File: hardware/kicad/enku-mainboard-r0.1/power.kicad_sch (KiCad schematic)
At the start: 5 parts

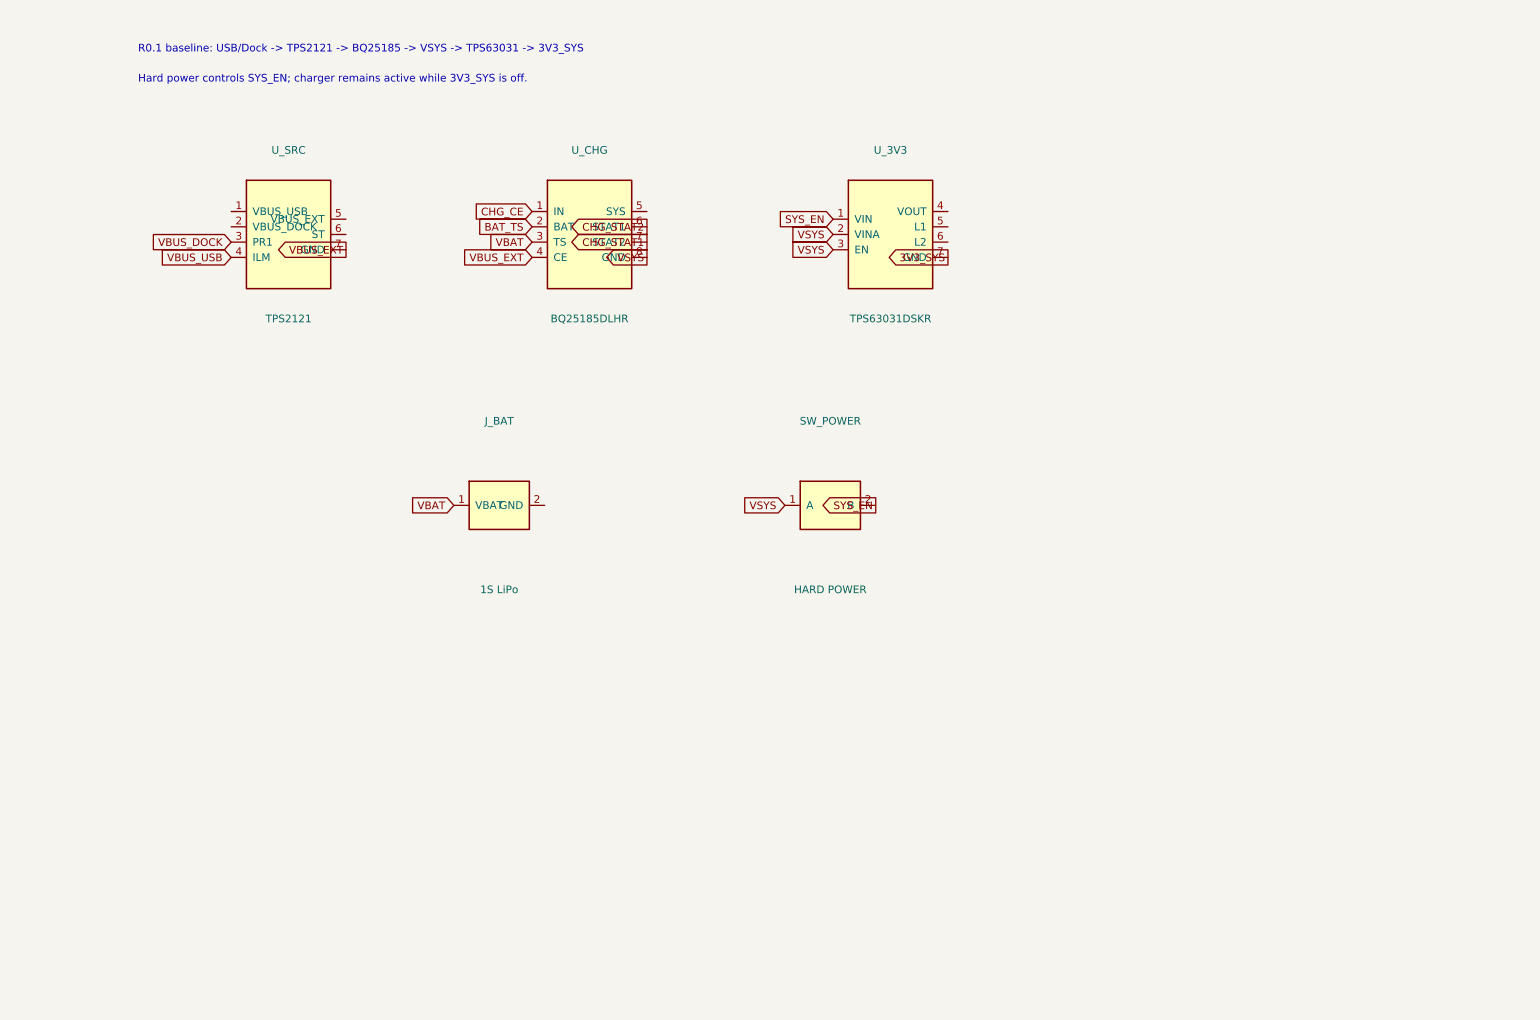
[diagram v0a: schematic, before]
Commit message: Expand R0.1 power sheet to exact IC pins and passives
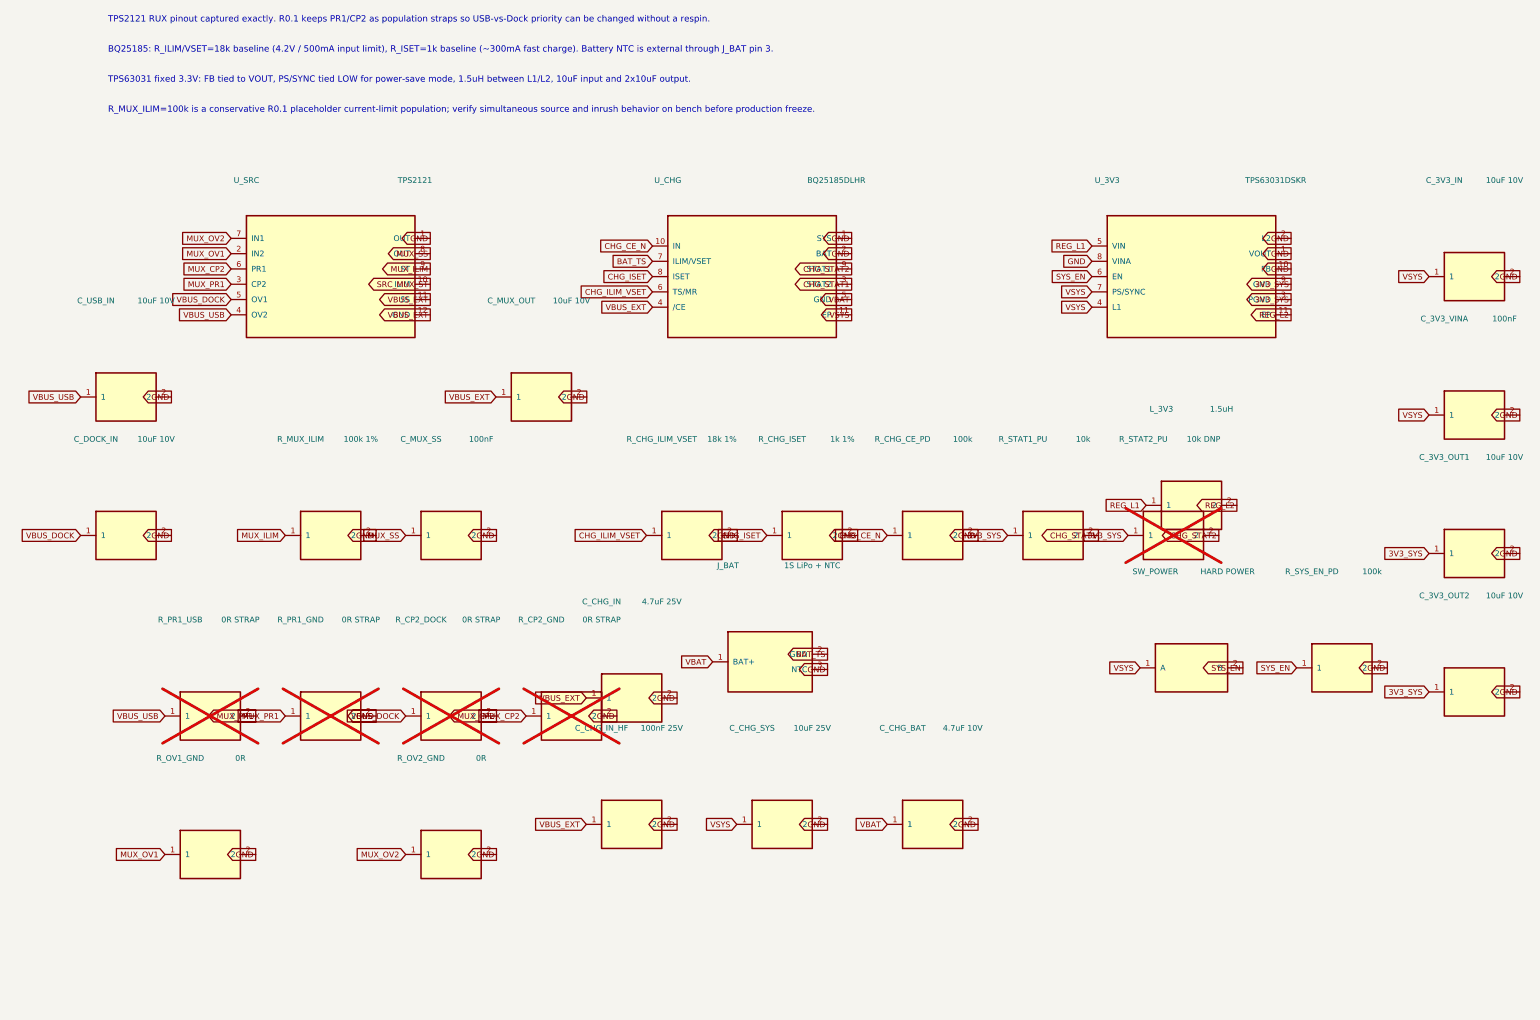
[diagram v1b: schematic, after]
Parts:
- removed J_BAT: 1S LiPo, Connector_JST:JST_PH_S2B-PH-SM4-TB_1x02-1MP_P2.00mm_Horizontal, symbol ENKU:BATTERY_2P
- removed SW_POWER: HARD POWER, Button_Switch_SMD:SW_SPDT_CK_JS102011SAQN, symbol ENKU:POWER_SWITCH
- removed U_3V3: TPS63031DSKR, Package_SON:WSON-10-1EP_2.5x2.5mm_P0.5mm_EP0.8x2mm, symbol ENKU:TPS63031_BLOCK
- removed U_CHG: BQ25185DLHR, Package_SON:Texas_DLH0010A, symbol ENKU:BQ25185_BLOCK
- removed U_SRC: TPS2121, Package_DFN_QFN:VQFN-HR-12-1EP_2.5x2.0mm_P0.5mm_EP0.6x1.6mm, symbol ENKU:TPS2121_BLOCK
- added C_3V3_IN, C_3V3_OUT1, C_3V3_OUT2, C_DOCK_IN, C_MUX_OUT, C_USB_IN: 10uF 10V, Capacitor_SMD:C_0805_2012Metric, symbol ENKU:C
- added C_3V3_VINA, C_MUX_SS: 100nF, Capacitor_SMD:C_0603_1608Metric, symbol ENKU:C
- added C_CHG_BAT: 4.7uF 10V, Capacitor_SMD:C_0805_2012Metric, symbol ENKU:C
- added C_CHG_IN: 4.7uF 25V, Capacitor_SMD:C_0805_2012Metric, symbol ENKU:C
- added C_CHG_IN_HF: 100nF 25V, Capacitor_SMD:C_0603_1608Metric, symbol ENKU:C
- added C_CHG_SYS: 10uF 25V, Capacitor_SMD:C_0805_2012Metric, symbol ENKU:C
- added J_BAT: 1S LiPo + NTC, Connector_Generic:Conn_01x03, symbol ENKU:BAT3
- added L_3V3: 1.5uH, Inductor_SMD:L_2520_HandSoldering, symbol ENKU:L
- added R_CHG_CE_PD, R_SYS_EN_PD: 100k, Resistor_SMD:R_0603_1608Metric, symbol ENKU:R
- added R_CHG_ILIM_VSET: 18k 1%, Resistor_SMD:R_0603_1608Metric, symbol ENKU:R
- added R_CHG_ISET: 1k 1%, Resistor_SMD:R_0603_1608Metric, symbol ENKU:R
- added R_CP2_DOCK, R_CP2_GND, R_PR1_GND, R_PR1_USB: 0R STRAP, Resistor_SMD:R_0603_1608Metric, symbol ENKU:R
- added R_MUX_ILIM: 100k 1%, Resistor_SMD:R_0603_1608Metric, symbol ENKU:R
- added R_OV1_GND, R_OV2_GND: 0R, Resistor_SMD:R_0603_1608Metric, symbol ENKU:R
- added R_STAT1_PU: 10k, Resistor_SMD:R_0603_1608Metric, symbol ENKU:R
- added R_STAT2_PU: 10k DNP, Resistor_SMD:R_0603_1608Metric, symbol ENKU:R
- added SW_POWER: HARD POWER, Button_Switch_SMD:SW_SPST, symbol ENKU:SW_SPST
- added U_3V3: TPS63031DSKR, ENKU:TPS63031_DSK0010A, symbol ENKU:TPS63031_DSK
- added U_CHG: BQ25185DLHR, ENKU:BQ25185_DLH0010A, symbol ENKU:BQ25185_DLH
- added U_SRC: TPS2121, ENKU:TPS2121_RUX0012B, symbol ENKU:TPS2121_RUX
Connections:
- net 3V3_SYS: now also C_3V3_OUT1.1, C_3V3_OUT2.1, R_STAT1_PU.1, R_STAT2_PU.1, U_3V3.3 (PGND), U_3V3.9 (GND)
- net BAT_TS: now also J_BAT.2 (GND), U_CHG.7 (ILIM/VSET)
- net CHG_STAT1: now also R_STAT1_PU.2, U_CHG.3 (STAT2)
- net CHG_STAT2: now also R_STAT2_PU.2, U_CHG.9 (STAT1)
- net SYS_EN: now also R_SYS_EN_PD.1, SW_POWER.2 (B), U_3V3.6 (EN)
- net VBAT: now also C_CHG_BAT.1, J_BAT.1 (BAT+), U_CHG.5 (GND)
- net VBUS_DOCK: now also C_DOCK_IN.1, R_CP2_DOCK.1, U_SRC.5 (OV1)
- net VBUS_EXT: now also C_CHG_IN.1, C_CHG_IN_HF.1, C_MUX_OUT.1, U_CHG.4 (/CE), U_SRC.11 (SS), U_SRC.12 (GND)
- net VBUS_USB: now also C_USB_IN.1, R_PR1_USB.1, U_SRC.4 (OV2)
- net VSYS: now also C_3V3_IN.1, C_3V3_VINA.1, C_CHG_SYS.1, SW_POWER.1 (A), U_3V3.4 (L1), U_3V3.7 (PS/SYNC), U_CHG.11 (EP)
- new net CHG_CE_N: R_CHG_CE_PD.1, U_CHG.10 (IN)
- new net CHG_ILIM_VSET: R_CHG_ILIM_VSET.1, U_CHG.6 (TS/MR)
- new net CHG_ISET: R_CHG_ISET.1, U_CHG.8 (ISET)
- new net GND: C_3V3_IN.2, C_3V3_OUT1.2, C_3V3_OUT2.2, C_3V3_VINA.2, C_CHG_BAT.2, C_CHG_IN.2, C_CHG_IN_HF.2, C_CHG_SYS.2, C_DOCK_IN.2, C_MUX_OUT.2, C_MUX_SS.2, C_USB_IN.2, J_BAT.3 (NTC), R_CHG_CE_PD.2, R_CHG_ILIM_VSET.2, R_CHG_ISET.2, R_CP2_GND.2, R_MUX_ILIM.2, R_OV1_GND.2, R_OV2_GND.2, R_PR1_GND.2, R_SYS_EN_PD.2, U_3V3.1 (VOUT), U_3V3.10 (FB), U_3V3.2 (L2), U_3V3.8 (VINA), U_CHG.1 (SYS), U_CHG.2 (BAT), U_SRC.1 (OUT)
- new net MUX_CP2: R_CP2_DOCK.2, R_CP2_GND.1, U_SRC.6 (PR1)
- new net MUX_ILIM: R_MUX_ILIM.1, U_SRC.9 (ST)
- new net MUX_OV1: R_OV1_GND.1, U_SRC.2 (IN2)
- new net MUX_OV2: R_OV2_GND.1, U_SRC.7 (IN1)
- new net MUX_PR1: R_PR1_GND.1, R_PR1_USB.2, U_SRC.3 (CP2)
- new net MUX_SS: C_MUX_SS.1, U_SRC.8 (OUT)
- new net REG_L1: L_3V3.1, U_3V3.5 (VIN)
- new net REG_L2: L_3V3.2, U_3V3.11 (EP)
- new net SRC_MUX_ST: U_SRC.10 (ILIM)
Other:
- note added: "BQ25185: R_ILIM/VSET=18k baseline (4.2V / 500mA input limit), R_ISET=1k baseline (~300mA fast charge). Battery NTC is external through J_BAT pin 3."
- note added: "R_MUX_ILIM=100k is a conservative R0.1 placeholder current-limit population; verify simultaneous source and inrush behavior on bench before production freeze."
- note added: "TPS2121 RUX pinout captured exactly. R0.1 keeps PR1/CP2 as population straps so USB-vs-Dock priority can be changed without a respin."
- note added: "TPS63031 fixed 3.3V: FB tied to VOUT, PS/SYNC tied LOW for power-save mode, 1.5uH between L1/L2, 10uF input and 2x10uF output."
- note removed: "Hard power controls SYS_EN; charger remains active while 3V3_SYS is off."
- note removed: "R0.1 baseline: USB/Dock -> TPS2121 -> BQ25185 -> VSYS -> TPS63031 -> 3V3_SYS"

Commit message: Upgrade R0.1 3V3 rail to TPS63802 high-current buck-boost
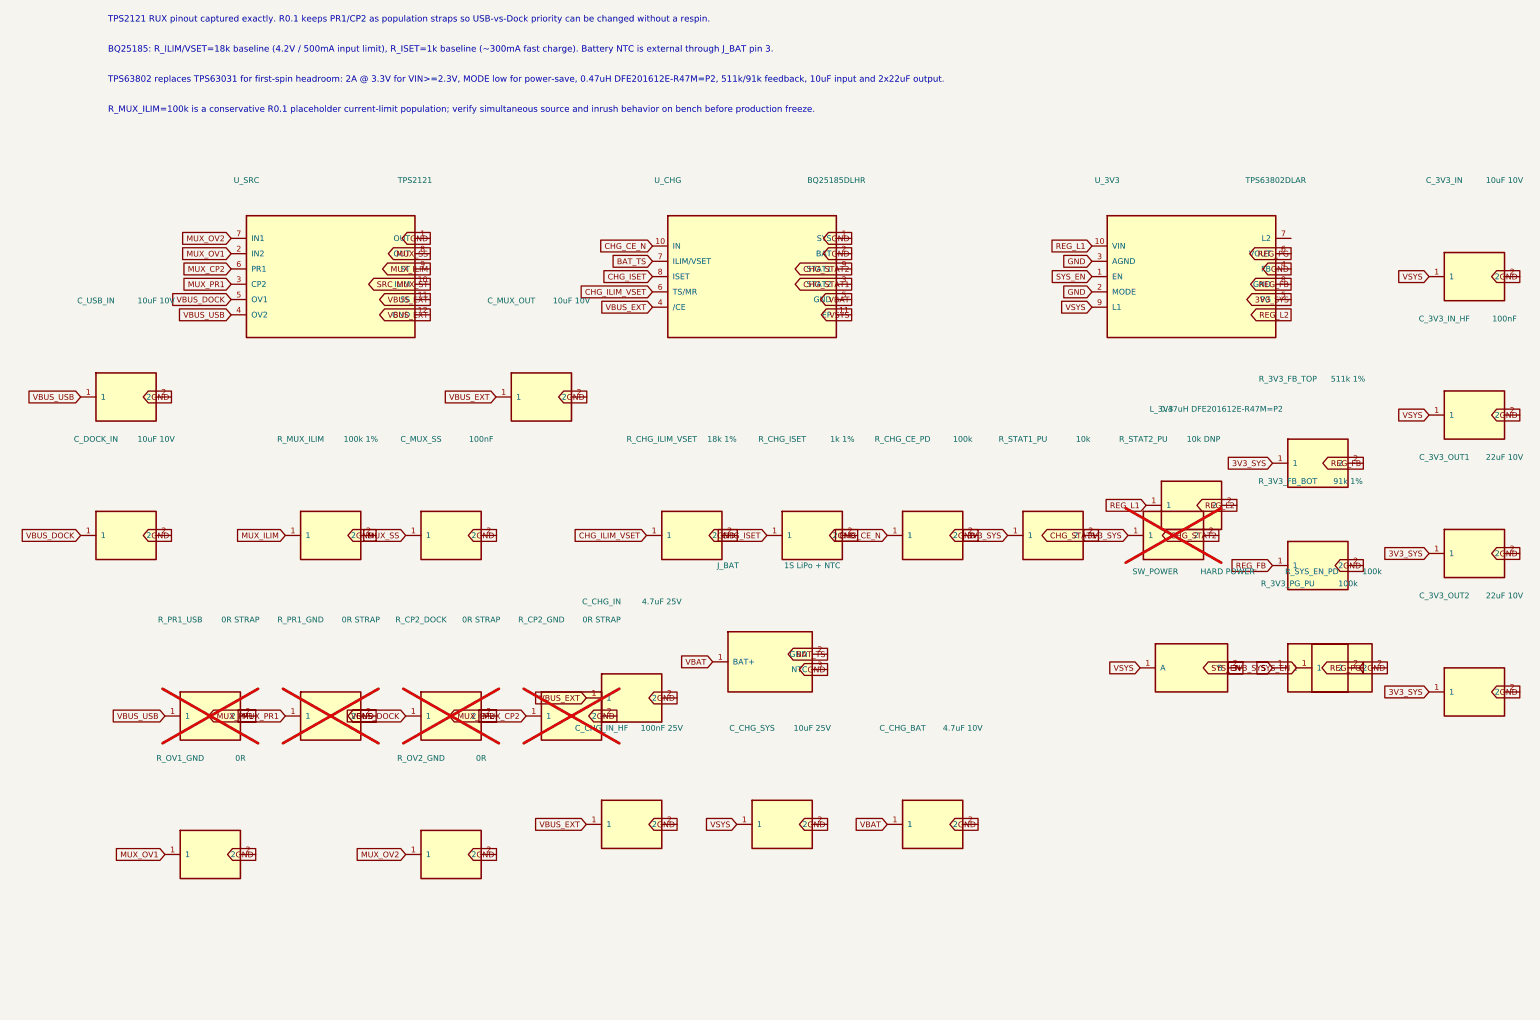
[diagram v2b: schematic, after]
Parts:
- added R_3V3_FB_BOT: 91k 1%, Resistor_SMD:R_0603_1608Metric, symbol ENKU:R
- added R_3V3_FB_TOP: 511k 1%, Resistor_SMD:R_0603_1608Metric, symbol ENKU:R
- added R_3V3_PG_PU: 100k, Resistor_SMD:R_0603_1608Metric, symbol ENKU:R
- C_3V3_OUT1, C_3V3_OUT2: value 10uF 10V -> 22uF 10V
- L_3V3: value 1.5uH -> 0.47uH DFE201612E-R47M=P2; footprint Inductor_SMD:L_2520_HandSoldering -> ENKU:Murata_DFE201612E
- U_3V3: value TPS63031DSKR -> TPS63802DLAR; footprint ENKU:TPS63031_DSK0010A -> ENKU:TPS63802_DLA0010A; symbol ENKU:TPS63031_DSK -> ENKU:TPS63802_DLA
- renumbered C_3V3_VINA to C_3V3_IN_HF
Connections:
- net 3V3_SYS: now also U_3V3.5 (PG), R_3V3_FB_TOP.1, R_3V3_PG_PU.1; no longer U_3V3.3 (PGND), U_3V3.9 (GND)
- net GND: now also U_3V3.3 (AGND), U_3V3.4 (FB), R_3V3_FB_BOT.2; no longer U_3V3.1 (VOUT), U_3V3.10 (FB), U_3V3.8 (VINA)
- net REG_L1: now also U_3V3.10 (VIN); no longer U_3V3.5 (VIN)
- net REG_L2: no longer U_3V3.11 (EP)
- net SYS_EN: now also U_3V3.1 (EN); no longer U_3V3.6 (EN)
- net VSYS: now also U_3V3.9 (L1); no longer U_3V3.4 (L1), U_3V3.7 (PS/SYNC)
- new net REG_FB: R_3V3_FB_BOT.1, R_3V3_FB_TOP.2, U_3V3.8 (GND)
- new net REG_PG: R_3V3_PG_PU.2, U_3V3.6 (VOUT)
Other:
- note added: "TPS63802 replaces TPS63031 for first-spin headroom: 2A @ 3.3V for VIN>=2.3V, MODE low for power-save, 0.47uH DFE201612E-R47M=P2, 511k/91k feedback, 10uF input and 2x22uF output."
- note removed: "TPS63031 fixed 3.3V: FB tied to VOUT, PS/SYNC tied LOW for power-save mode, 1.5uH between L1/L2, 10uF input and 2x10uF output."
